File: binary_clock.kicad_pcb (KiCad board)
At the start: 2 copper layers, 30 parts, among them P1 USB_C_Plug_USB2.0, SW1 RESET, SW2 BOOTSEL, U1 RP2040, U2 W25Q32JVSS, U3 AMS1117-3.3, Y1 Crystal_GND23

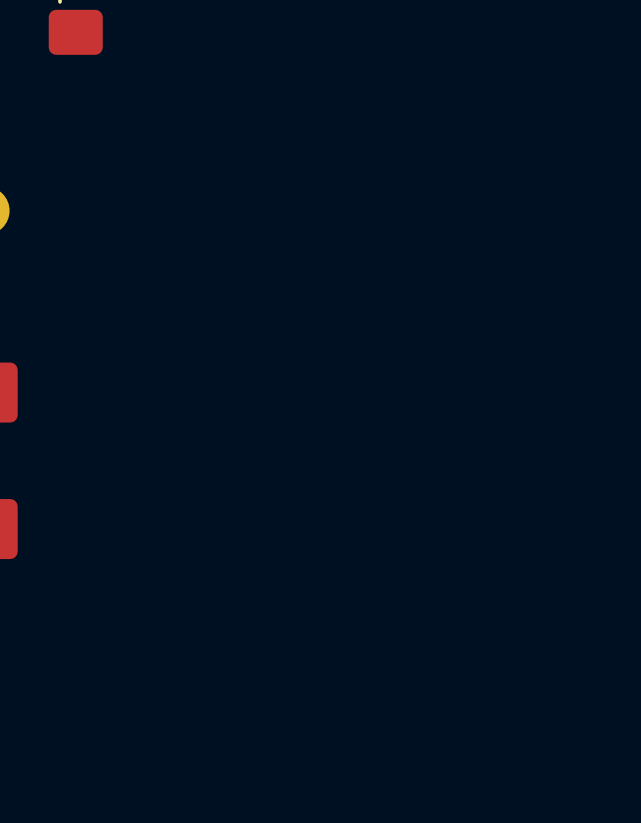
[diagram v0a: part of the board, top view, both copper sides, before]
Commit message: added switches and labels for i2c0
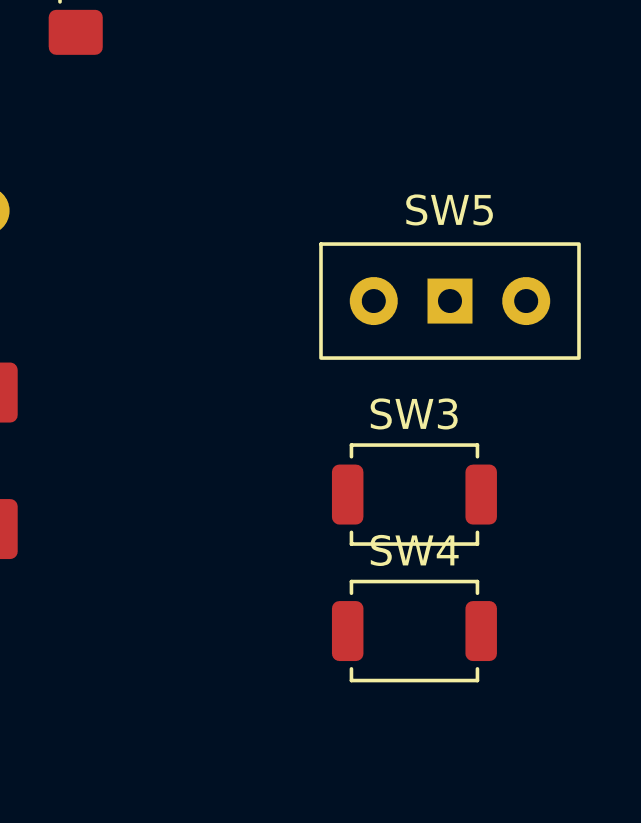
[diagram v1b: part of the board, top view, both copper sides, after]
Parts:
- added SW3: BACKWARD, Button_Switch_SMD:SW_SPST_TS-1088-xR020, F.Cu at (151.3, 123.0)
- added SW4: FORWARD, Button_Switch_SMD:SW_SPST_TS-1088-xR020, F.Cu at (151.3, 127.5)
- added SW5: TIMEZONE_CHANGE, switch:SW_Slide_8.6x3.8x7.0_P2.54mm, F.Cu at (152.5, 116.5)
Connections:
- U1 pad 4: unconnected-(U1-GPIO2-Pad4) -> Net-(U1-GPIO2)
- U1 pad 5: unconnected-(U1-GPIO3-Pad5) -> Net-(U1-GPIO3)
- U1 pad 6: unconnected-(U1-GPIO4-Pad6) -> /SDA
- U1 pad 7: unconnected-(U1-GPIO5-Pad7) -> /SCL
- U1 pad 8: unconnected-(U1-GPIO6-Pad8) -> Net-(SW5-B)

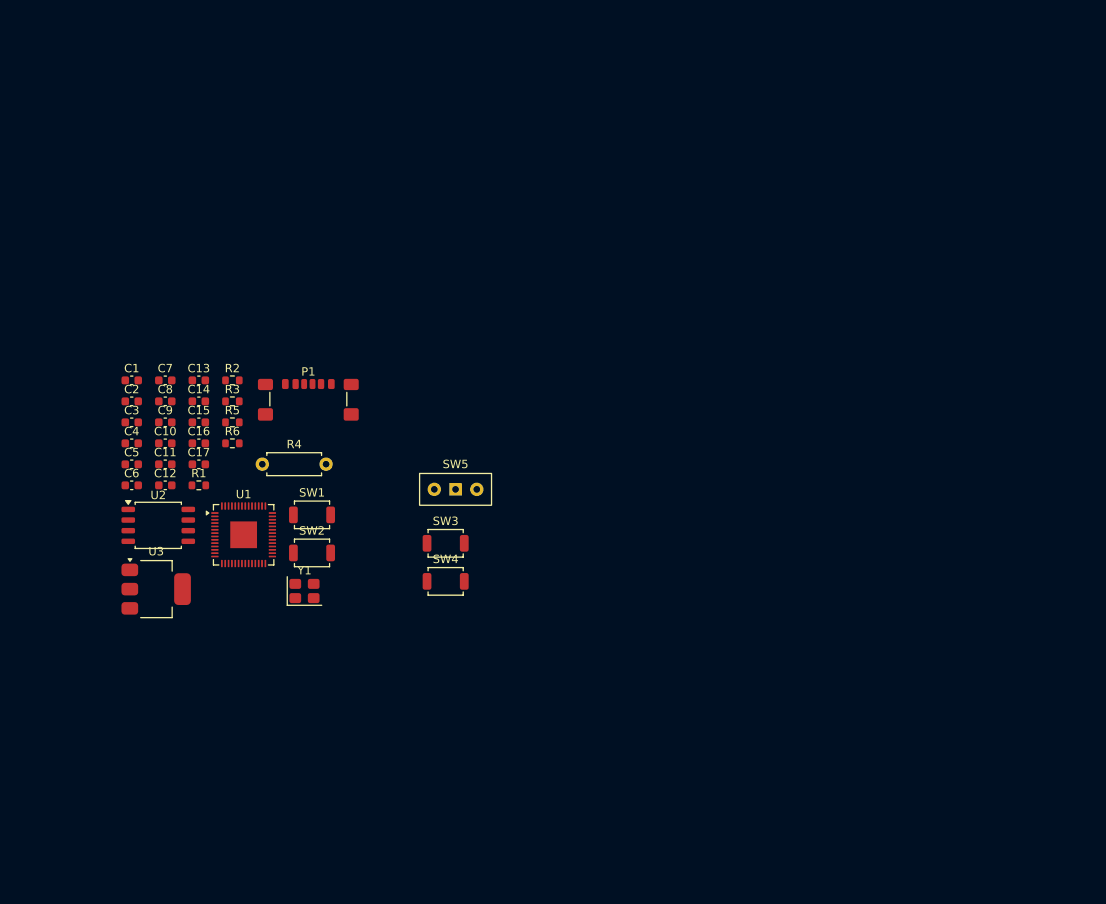
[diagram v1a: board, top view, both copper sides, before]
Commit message: half pcb done and cutouts
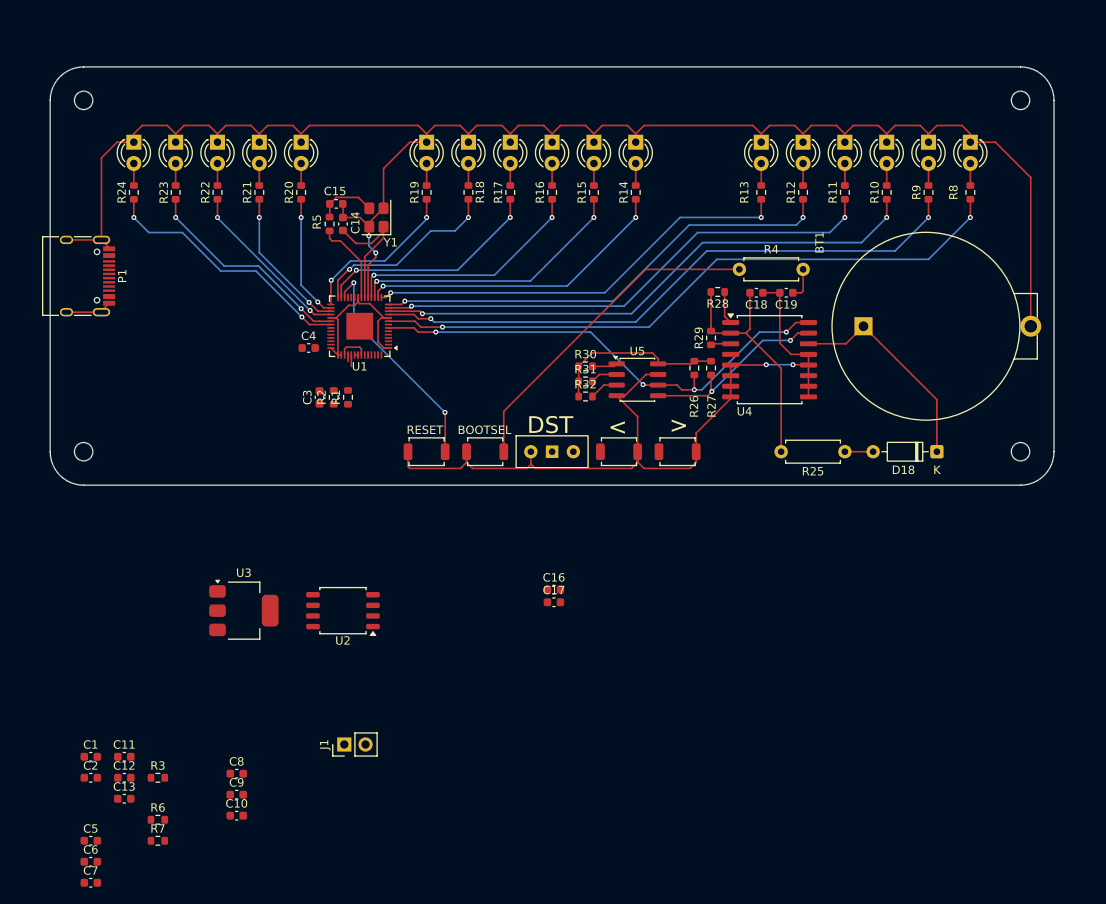
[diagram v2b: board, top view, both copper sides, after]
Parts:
- added 0: MountingHole_2.2mm_M2_DIN965, MountingHole:MountingHole_2.2mm_M2_DIN965, F.Cu at (220.0, 112.0)
- added 0: MountingHole_2.2mm_M2_DIN965, MountingHole:MountingHole_2.2mm_M2_DIN965, F.Cu at (220.0, 70.0)
- added 0: MountingHole_2.2mm_M2_DIN965, MountingHole:MountingHole_2.2mm_M2_DIN965, F.Cu at (108.0, 70.0)
- added 0: MountingHole_2.2mm_M2_DIN965, MountingHole:MountingHole_2.2mm_M2_DIN965, F.Cu at (108.0, 112.0)
- added BT1: CR2032_holder, custom_footprints:Battery_Holder_Coin_2032_BS-7, F.Cu at (201.2, 97.0)
- added C18: 100n, Capacitor_SMD:C_0603_1608Metric, F.Cu at (188.4, 93.0)
- added C19: 1u, Capacitor_SMD:C_0603_1608Metric, F.Cu at (192.0, 93.0)
- added D1: LED, LED_THT:LED_D3.0mm, F.Cu at (214.0, 75.0)
- added D10: LED, LED_THT:LED_D3.0mm, F.Cu at (159.0, 75.0)
- added D11: LED, LED_THT:LED_D3.0mm, F.Cu at (154.0, 75.0)
- added D12: LED, LED_THT:LED_D3.0mm, F.Cu at (149.0, 75.0)
- added D13: LED, LED_THT:LED_D3.0mm, F.Cu at (134.0, 75.0)
- added D14: LED, LED_THT:LED_D3.0mm, F.Cu at (129.0, 75.0)
- added D15: LED, LED_THT:LED_D3.0mm, F.Cu at (124.0, 75.0)
- added D16: LED, LED_THT:LED_D3.0mm, F.Cu at (119.0, 75.0)
- added D17: LED, LED_THT:LED_D3.0mm, F.Cu at (114.0, 75.0)
- added D18: 1N4148, Diode_THT:D_DO-35_SOD27_P7.62mm_Horizontal, F.Cu at (210.0, 112.0)
- added D2: LED, LED_THT:LED_D3.0mm, F.Cu at (209.0, 75.0)
- added D3: LED, LED_THT:LED_D3.0mm, F.Cu at (204.0, 75.0)
- added D4: LED, LED_THT:LED_D3.0mm, F.Cu at (199.0, 75.0)
- added D5: LED, LED_THT:LED_D3.0mm, F.Cu at (194.0, 75.0)
- added D6: LED, LED_THT:LED_D3.0mm, F.Cu at (189.0, 75.0)
- added D7: LED, LED_THT:LED_D3.0mm, F.Cu at (174.0, 75.0)
- added D8: LED, LED_THT:LED_D3.0mm, F.Cu at (169.0, 75.0)
- added D9: LED, LED_THT:LED_D3.0mm, F.Cu at (164.0, 75.0)
- added J1: Conn_01x02_Socket, Connector_PinHeader_2.54mm:PinHeader_1x02_P2.54mm_Vertical, F.Cu at (139.2, 147.0)
- added R10: 1k, Resistor_SMD:R_0603_1608Metric, F.Cu at (204.0, 81.0)
- added R11: 1k, Resistor_SMD:R_0603_1608Metric, F.Cu at (199.0, 81.0)
- added R12: 1k, Resistor_SMD:R_0603_1608Metric, F.Cu at (194.0, 81.0)
- added R13: 1k, Resistor_SMD:R_0603_1608Metric, F.Cu at (189.0, 81.0)
- added R14: 1k, Resistor_SMD:R_0603_1608Metric, F.Cu at (174.0, 81.0)
- added R15: 1k, Resistor_SMD:R_0603_1608Metric, F.Cu at (169.0, 81.0)
- added R16: 1k, Resistor_SMD:R_0603_1608Metric, F.Cu at (164.0, 81.0)
- added R17: 1k, Resistor_SMD:R_0603_1608Metric, F.Cu at (159.0, 81.0)
- added R18: 1k, Resistor_SMD:R_0603_1608Metric, F.Cu at (154.0, 81.0)
- added R19: 1k, Resistor_SMD:R_0603_1608Metric, F.Cu at (149.0, 81.0)
- added R20: 1k, Resistor_SMD:R_0603_1608Metric, F.Cu at (134.0, 81.0)
- added R21: 1k, Resistor_SMD:R_0603_1608Metric, F.Cu at (129.0, 81.0)
- added R22: 1k, Resistor_SMD:R_0603_1608Metric, F.Cu at (124.0, 81.0)
- added R23: 1k, Resistor_SMD:R_0603_1608Metric, F.Cu at (119.0, 81.0)
- added R24: 1k, Resistor_SMD:R_0603_1608Metric, F.Cu at (114.0, 81.0)
- added R25: 1k, Resistor_THT:R_Axial_DIN0207_L6.3mm_D2.5mm_P7.62mm_Horizontal, F.Cu at (199.0, 112.0)
- added R26: 4k7, Resistor_SMD:R_0603_1608Metric, F.Cu at (181.0, 102.0)
- added R27: 4k7, Resistor_SMD:R_0603_1608Metric, F.Cu at (183.0, 102.0)
- added R28: 4k7, Resistor_SMD:R_0603_1608Metric, F.Cu at (183.8, 92.9)
- added R29: 4k7, Resistor_SMD:R_0603_1608Metric, F.Cu at (183.0, 98.4)
- added R30: 4k7, Resistor_SMD:R_0603_1608Metric, F.Cu at (168.0, 101.8)
- added R31: 4k7, Resistor_SMD:R_0603_1608Metric, F.Cu at (168.0, 103.6)
- added R32: 4k7, Resistor_SMD:R_0603_1608Metric, F.Cu at (168.0, 105.4)
- added R7: 5k1, Resistor_SMD:R_0603_1608Metric, F.Cu at (116.9, 158.5)
- added R8: 1k, Resistor_SMD:R_0603_1608Metric, F.Cu at (214.0, 81.0)
- added R9: 1k, Resistor_SMD:R_0603_1608Metric, F.Cu at (209.0, 81.0)
- added U4: DS3231M, Package_SO:SOIC-16W_7.5x10.3mm_P1.27mm, F.Cu at (190.0, 101.0)
- added U5: AT24C32_SOIC, Package_SO:SOIC-8_3.9x4.9mm_P1.27mm, F.Cu at (174.2, 103.4)
- P1: value USB_C_Plug_USB2.0 -> USB_C-31-M-12; footprint Connector_USB:USB_C_Receptacle_GCT_USB4135-GF-A_6P_TopMnt_Horizontal -> Connector_USB:USB_C_Receptacle_HRO_TYPE-C-31-M-12
- SW5: footprint switch:SW_Slide_8.6x3.8x7.0_P2.54mm -> custom_footprints:SW_Slide_8.6x3.8x7.0_P2.54mm
- moved R4 61.6 mm to (186.4, 90.2)
- moved C7 60.7 mm to (108.9, 163.5)
- moved C13 50.8 mm to (112.9, 153.5)
- moved C16 45.9 mm to (164.2, 128.5)
- moved R6 45.9 mm to (116.9, 156.0)
- moved R3 45.9 mm to (116.9, 151.0)
- moved C17 45.5 mm to (164.2, 130.0)
- moved Y1 45.5 mm to (143.0, 84.0), turned to 90 degrees
- moved C8 45.3 mm to (126.3, 150.5)
- moved C9 45.3 mm to (126.3, 153.0)
- moved C10 45.3 mm to (126.3, 155.5)
- moved C6 45.3 mm to (108.9, 161.0)
- moved C1 45.3 mm to (108.9, 148.5)
- moved C2 45.3 mm to (108.9, 151.0)
- moved C5 45.3 mm to (108.9, 158.5)
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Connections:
- P1 pad B5: unconnected-(P1-VCONN-PadB5) -> Net-(P1-CC2)
- U1 pad 11: unconnected-(U1-GPIO8-Pad11) -> Net-(U1-GPIO8)
- U1 pad 12: unconnected-(U1-GPIO9-Pad12) -> Net-(U1-GPIO9)
- U1 pad 13: unconnected-(U1-GPIO10-Pad13) -> Net-(U1-GPIO10)
- U1 pad 14: unconnected-(U1-GPIO11-Pad14) -> Net-(U1-GPIO11)
- U1 pad 15: unconnected-(U1-GPIO12-Pad15) -> Net-(U1-GPIO12)
- U1 pad 16: unconnected-(U1-GPIO13-Pad16) -> Net-(U1-GPIO13)
- U1 pad 17: unconnected-(U1-GPIO14-Pad17) -> Net-(U1-GPIO14)
- U1 pad 18: unconnected-(U1-GPIO15-Pad18) -> Net-(U1-GPIO15)
- U1 pad 2: unconnected-(U1-GPIO0-Pad2) -> /TX
- U1 pad 27: unconnected-(U1-GPIO16-Pad27) -> Net-(U1-GPIO16)
- U1 pad 28: unconnected-(U1-GPIO17-Pad28) -> Net-(U1-GPIO17)
- U1 pad 29: unconnected-(U1-GPIO18-Pad29) -> Net-(U1-GPIO18)
- U1 pad 3: unconnected-(U1-GPIO1-Pad3) -> /RX
- U1 pad 30: unconnected-(U1-GPIO19-Pad30) -> Net-(U1-GPIO19)
- U1 pad 31: unconnected-(U1-GPIO20-Pad31) -> Net-(U1-GPIO20)
- U1 pad 32: unconnected-(U1-GPIO21-Pad32) -> Net-(U1-GPIO21)
- U1 pad 34: unconnected-(U1-GPIO22-Pad34) -> Net-(U1-GPIO22)
- U1 pad 35: unconnected-(U1-GPIO23-Pad35) -> Net-(U1-GPIO23)
- U1 pad 9: unconnected-(U1-GPIO7-Pad9) -> Net-(U1-GPIO7)
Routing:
- net GND: track 0.00 -> 308.8 mm, vias 0 -> 4
- net Net-(U1-GPIO7): track 0.00 -> 77.5 mm, vias 0 -> 2
- net +3.3V: track 0.00 -> 75.3 mm
- net Net-(U1-GPIO8): track 0.00 -> 72.3 mm, vias 0 -> 2
- net Net-(U1-GPIO9): track 0.00 -> 66.6 mm, vias 0 -> 2
- net Net-(U1-GPIO10): track 0.00 -> 61.2 mm, vias 0 -> 2
- net /SCL: track 0.00 -> 58.4 mm, vias 0 -> 4
- net Net-(U1-GPIO11): track 0.00 -> 56.1 mm, vias 0 -> 2
- net Net-(U1-GPIO12): track 0.00 -> 51.5 mm, vias 0 -> 2
- net Net-(R3-Pad1): track 0.00 -> 40.0 mm
- net Net-(U1-GPIO13): track 0.00 -> 37.4 mm, vias 0 -> 2
- net Net-(U1-GPIO14): track 0.00 -> 33.4 mm, vias 0 -> 2
- net Net-(U1-GPIO23): track 0.00 -> 31.0 mm, vias 0 -> 2
- net Net-(U1-GPIO15): track 0.00 -> 29.1 mm, vias 0 -> 2
- net Net-(U1-GPIO16): track 0.00 -> 27.2 mm, vias 0 -> 2
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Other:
- board outline added: 120 x 50 mm
- board text added: ">"
- board text added: "BOOTSEL"
- board text added: "DST"
- board text added: "RESET"

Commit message: pcb finished
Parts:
- moved R6 72.7 mm to (106.8, 84.0), turned to 180 degrees
- moved R7 61.3 mm to (106.8, 98.0), turned to 180 degrees
- moved C16 58.8 mm to (111.2, 103.0), turned to -90 degrees
- moved C2 56.4 mm to (129.6, 98.5), turned to -90 degrees
- moved C12 56.2 mm to (149.0, 108.0), turned to 180 degrees
- moved C1 54.8 mm to (131.3, 98.5), turned to -90 degrees
- moved C7 53.6 mm to (124.5, 112.3), turned to 90 degrees
- moved C17 50.9 mm to (121.1, 103.0), turned to -90 degrees
- moved C6 50.7 mm to (122.9, 112.3), turned to 90 degrees
- moved R3 48.2 mm to (149.0, 115.0), turned to 180 degrees
- moved C5 47.9 mm to (121.3, 112.3), turned to 90 degrees
- moved C13 45.5 mm to (133.6, 113.0)
- moved C10 43.3 mm to (129.3, 112.3), turned to 90 degrees
- moved J1 43.1 mm to (147.7, 104.8)
- moved C9 40.7 mm to (127.7, 112.3), turned to 90 degrees
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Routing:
- net +3.3V: track 75.3 -> 178.0 mm, vias 0 -> 9
- net GND: track 308.8 -> 407.3 mm, vias 4 -> 12
- net Net-(U1-GPIO3): track 0.00 -> 40.5 mm, vias 0 -> 2
- net /SDA: track 23.1 -> 61.0 mm, vias 2 -> 4
- net Net-(SW5-B): track 0.00 -> 35.0 mm, vias 0 -> 2
- net Net-(U1-GPIO2): track 0.00 -> 32.6 mm, vias 0 -> 2
- net /USB_DM: track 0.00 -> 31.8 mm
- net /USB_DP: track 0.00 -> 30.8 mm
- net Net-(U3-VI): track 0.00 -> 23.5 mm, vias 0 -> 2
- net Net-(R3-Pad1): track 40.0 -> 61.5 mm, vias 0 -> 3
- net /QSPI_SS: track 0.00 -> 20.2 mm, vias 0 -> 2
- net Net-(U1-VREG_VOUT): track 3.64 -> 21.9 mm, vias 0 -> 4
- net /QSPI_SD1: track 0.00 -> 14.6 mm, vias 0 -> 2
- net /QSPI_SD3: track 0.00 -> 14.3 mm, vias 0 -> 2
- net /QSPI_SD2: track 0.00 -> 14.1 mm, vias 0 -> 2
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- added copper zone on B.Cu, net GND
- added copper zone on F.Cu, net GND
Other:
- board text added: "RX"
- board text added: "TX"

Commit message: final pcb, ignore production/
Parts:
- J1: value Conn_01x02_Socket -> Conn_01x03_Pin; footprint Connector_PinHeader_2.54mm:PinHeader_1x02_P2.54mm_Vertical -> Connector_PinHeader_2.54mm:PinHeader_1x03_P2.54mm_Vertical
- P1: value USB_C-31-M-12 -> TYPE-C-31-M-12
- R1, R2: value 27 -> 33
- SW1: value RESET -> TS-1088-AR02016
- SW2: value BOOTSEL -> TS-1088-AR02016
- SW3: value BACKWARD -> TS-1088-AR02016
- SW4: value FORWARD -> TS-1088-AR02016
- Y1: value Crystal_GND23 -> ABM8-272-T3
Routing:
- net GND: track 407.3 -> 414.9 mm
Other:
- board text added: "GND"
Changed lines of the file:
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@@
 			)
 		)
-		(property "Value" "Crystal_GND23"
+		(property "Value" "ABM8-272-T3"
 			(at 0.1 3.15 90)
 			(layer "F.Fab")
@@
 		)
 	)
-	(footprint "Connector_PinHeader_2.54mm:PinHeader_1x02_P2.54mm_Vertical"
+	(footprint "Connector_PinHeader_2.54mm:PinHeader_1x03_P2.54mm_Vertical"
 		(layer "F.Cu")
 		(at 147.725 104.8 90)
-		(descr "Through hole straight pin header, 1x02, 2.54mm pitch, single row")
-		(tags "Through hole pin header THT 1x02 2.54mm single row")
+		(descr "Through hole straight pin header, 1x03, 2.54mm pitch, single row")
+		(tags "Through hole pin header THT 1x03 2.54mm single row")
 		(property "Reference" "J1"
-			(at -2.5 -1.025 180)
+			(at 0 -2.38 90)
 			(layer "F.SilkS")
 			(hide yes)
@@
 			)
 		)
-		(property "Value" "Conn_01x02_Socket"
-			(at -3 -1 180)
+		(property "Value" "Conn_01x03_Pin"
+			(at 0 7.46 90)
 			(layer "F.Fab")
 			(effects
@@
 			)
 		)
-		(property "Description" "Generic connector, single row, 01x02, script generated"
+		(property "Description" "Generic connector, single row, 01x03, script generated"
 			(at 0 0 90)
 			(layer "F.Fab")
@@
 		(attr through_hole)
 		(fp_line
-			(start -1.38 -1.38)
-			(end 0 -1.38)
+			(start 1.4 -1.395)
+			(end 1.4 3.795)
 			(stroke
 				(width 0.12)
@@
 		)
 		(fp_line
-			(start -1.38 0)
-			(end -1.38 -1.38)
+			(start -1.36 -1.395)
+			(end 1.4 -1.395)
 			(stroke
 				(width 0.12)
@@
 		)
 		(fp_line
-			(start 1.38 1.27)
-			(end 1.38 3.92)
+			(start -1.36 -1.395)
+			(end -1.36 3.795)
 			(stroke
 				(width 0.12)
@@
 		)
 		(fp_line
-			(start -1.38 1.27)
-			(end 1.38 1.27)
-			(stroke
-				(width 0.12)
-				(type solid)
-			)
-			(layer "F.SilkS")
-		)
-		(fp_line
-			(start -1.38 1.27)
-			(end -1.38 3.92)
-			(stroke
-				(width 0.12)
-				(type solid)
-			)
-			(layer "F.SilkS")
-		)
-		(fp_line
-			(start -1.38 3.92)
-			(end 1.38 3.92)
+			(start -1.36 3.795)
+			(end 1.4 3.795)
 			(stroke
 				(width 0.12)
@@
 		(fp_line
 			(start -1.77 -1.77)
-			(end -1.77 4.32)
+			(end -1.77 6.85)
 			(stroke
 				(width 0.05)
@@
 		)
 		(fp_line
-			(start 1.77 4.32)
+			(start 1.77 6.85)
 			(end 1.77 -1.77)
 			(stroke
@@
 		)
 		(fp_line
-			(start -1.77 4.32)
-			(end 1.77 4.32)
+			(start -1.77 6.85)
+			(end 1.77 6.85)
 			(stroke
 				(width 0.05)
@@
 		(fp_line
 			(start 1.27 -1.27)
-			(end 1.27 3.81)
+			(end 1.27 6.35)
 			(stroke
 				(width 0.1)
@@
 		)
 		(fp_line
-			(start 1.27 3.81)
-			(end -1.27 3.81)
+			(start 1.27 6.35)
+			(end -1.27 6.35)
 			(stroke
 				(width 0.1)
@@
 		)
 		(fp_line
-			(start -1.27 3.81)
+			(start -1.27 6.35)
 			(end -1.27 -0.635)
 			(stroke
@@
 		)
 		(fp_text user "${REFERENCE}"
-			(at 0 1.27 0)
+			(at 0 2.54 180)
 			(layer "F.Fab")
 			(effects
@@
 			)
 		)
-		(pad "1" thru_hole rect
+		(pad "1" thru_hole circle
 			(at 0 0 90)
 			(size 1.7 1.7)
@@
 			(pintype "passive")
 		)
+		(pad "3" thru_hole rect
+			(at 0 5.08 90)
+			(size 1.7 1.7)
+			(drill 1)
+			(layers "*.Cu" "*.Mask")
+			(remove_unused_layers no)
+			(net 1 "GND")
+			(pinfunction "Pin_3")
+			(pintype "passive")
+		)
 		(embedded_fonts no)
-		(model "${KICAD9_3DMODEL_DIR}/Connector_PinHeader_2.54mm.3dshapes/PinHeader_1x02_P2.54mm_Vertical.step"
+		(model "${KICAD9_3DMODEL_DIR}/Connector_PinHeader_2.54mm.3dshapes/PinHeader_1x03_P2.54mm_Vertical.step"
 			(offset
 				(xyz 0 0 0)
@@
 			)
 		)
-		(property "Value" "USB_C-31-M-12"
+		(property "Value" "TYPE-C-31-M-12"
 			(at 0 5.1 90)
 			(layer "F.Fab")
@@
 			)
 		)
-		(property "Value" "BACKWARD"
+		(property "Value" "TS-1088-AR02016"
 			(at 0 2.65 0)
 			(layer "F.Fab")
@@
 			)
 		)
-		(property "Value" "27"
+		(property "Value" "33"
 			(at 0 1.43 0)
 			(layer "F.Fab")
@@
 			)
 		)
-		(property "Value" "27"
+		(property "Value" "33"
 			(at 0 1.43 0)
 			(layer "F.Fab")
@@
 		(sheetname "/")
 		(sheetfile "binary_clock.kicad_sch")
-		(attr through_hole)
+		(attr through_hole dnp)
 		(fp_line
 			(start 0.54 -1.37)
@@
 			)
 		)
-		(property "Value" "FORWARD"
+		(property "Value" "TS-1088-AR02016"
 			(at 0 2.65 0)
 			(layer "F.Fab")
@@
 			)
 		)
-		(property "Value" "RESET"
+		(property "Value" "TS-1088-AR02016"
 			(at 0 2.65 0)
 			(layer "F.Fab")
@@
 			)
 		)
-		(property "Value" "BOOTSEL"
+		(property "Value" "TS-1088-AR02016"
 			(at 0 2.65 0)
 			(layer "F.Fab")
@@
 		)
 	)
+	(gr_text "GND"
+		(at 152.8 107.8 0)
+		(layer "F.SilkS")
+		(effects
+			(font
+				(size 1 1)
+				(thickness 0.1)
+			)
+			(justify left bottom)
+		)
+	)
 	(gr_text "DST"
 		(at 161 110 0)
@@
 	)
 	(segment
+		(start 152.805 104.8)
+		(end 153.775 105.77)
+		(width 0.2)
+		(layer "F.Cu")
+		(net 1)
+	)
+	(segment
 		(start 111.045 87.595)
 		(end 110.13 86.68)
@@
 	)
 	(segment
+		(start 153.775 105.77)
+		(end 153.775 112)
+		(width 0.2)
+		(layer "F.Cu")
+		(net 1)
+	)
+	(segment
 		(start 165 73)
 		(end 164 74)
@@
 	)
 	(segment
-		(start 156.9 107)
-		(end 149.4 99.5)
+		(start 164.35 107)
+		(end 156.85 99.5)
 		(width 0.2)
 		(layer "B.Cu")
@@
 	)
 	(segment
-		(start 189.2 98.7)
-		(end 183.1 104.8)
+		(start 176.7 107)
+		(end 164.35 107)
 		(width 0.2)
 		(layer "B.Cu")
@@
 	)
 	(segment
-		(start 176.7 107)
-		(end 156.9 107)
+		(start 156.85 99.5)
+		(end 149.4 99.5)
+		(width 0.2)
+		(layer "B.Cu")
+		(net 58)
+	)
+	(segment
+		(start 189.2 98.7)
+		(end 183.1 104.8)
 		(width 0.2)
 		(layer "B.Cu")
@@
 	(segment
 		(start 169.8 109.2)
-		(end 157 109.2)
+		(end 164.1 109.2)
+		(width 0.2)
+		(layer "B.Cu")
+		(net 64)
+	)
+	(segment
+		(start 164.1 109.2)
+		(end 157.2 102.3)
 		(width 0.2)
 		(layer "B.Cu")
@@
 	)
 	(segment
-		(start 157 109.2)
+		(start 157.2 102.3)
 		(end 150.1 102.3)
 		(width 0.2)
@@
 	)
 	(segment
+		(start 164.2 108.1)
+		(end 156.9 100.8)
+		(width 0.2)
+		(layer "B.Cu")
+		(net 65)
+	)
+	(segment
 		(start 176.8 108.1)
-		(end 157 108.1)
+		(end 164.2 108.1)
 		(width 0.2)
 		(layer "B.Cu")
@@
 	)
 	(segment
-		(start 157 108.1)
+		(start 156.9 100.8)
 		(end 149.7 100.8)
 		(width 0.2)

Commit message: cr2032 holder footprint fix, gitignore build
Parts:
- BT1: value CR2032_holder -> CR2032
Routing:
- net Net-(BT1-+): track 26.1 -> 49.7 mm
- net GND: track 414.9 -> 420.4 mm
